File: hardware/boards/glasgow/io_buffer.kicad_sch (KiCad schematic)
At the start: 68 parts, among them J2 IDC-Header_2x10_P2.54mm, J8 Conn_01x08, J9 Conn_01x08, U10 SN74LVC1T45DCKR, U11 SN74LVC1T45DCKR, U16 SN74LVC1T45DCKR, U17 SN74LVC1T45DCKR, U18 SN74LVC1T45DCKR, U19 PCA6408APW, U20 DAC081C081CIMK, U21 INA233, U31 TPS73101DBV, U4 SN74LVC1T45DCKR, U6 SN74LVC1T45DCKR, U9 SN74LVC1T45DCKR

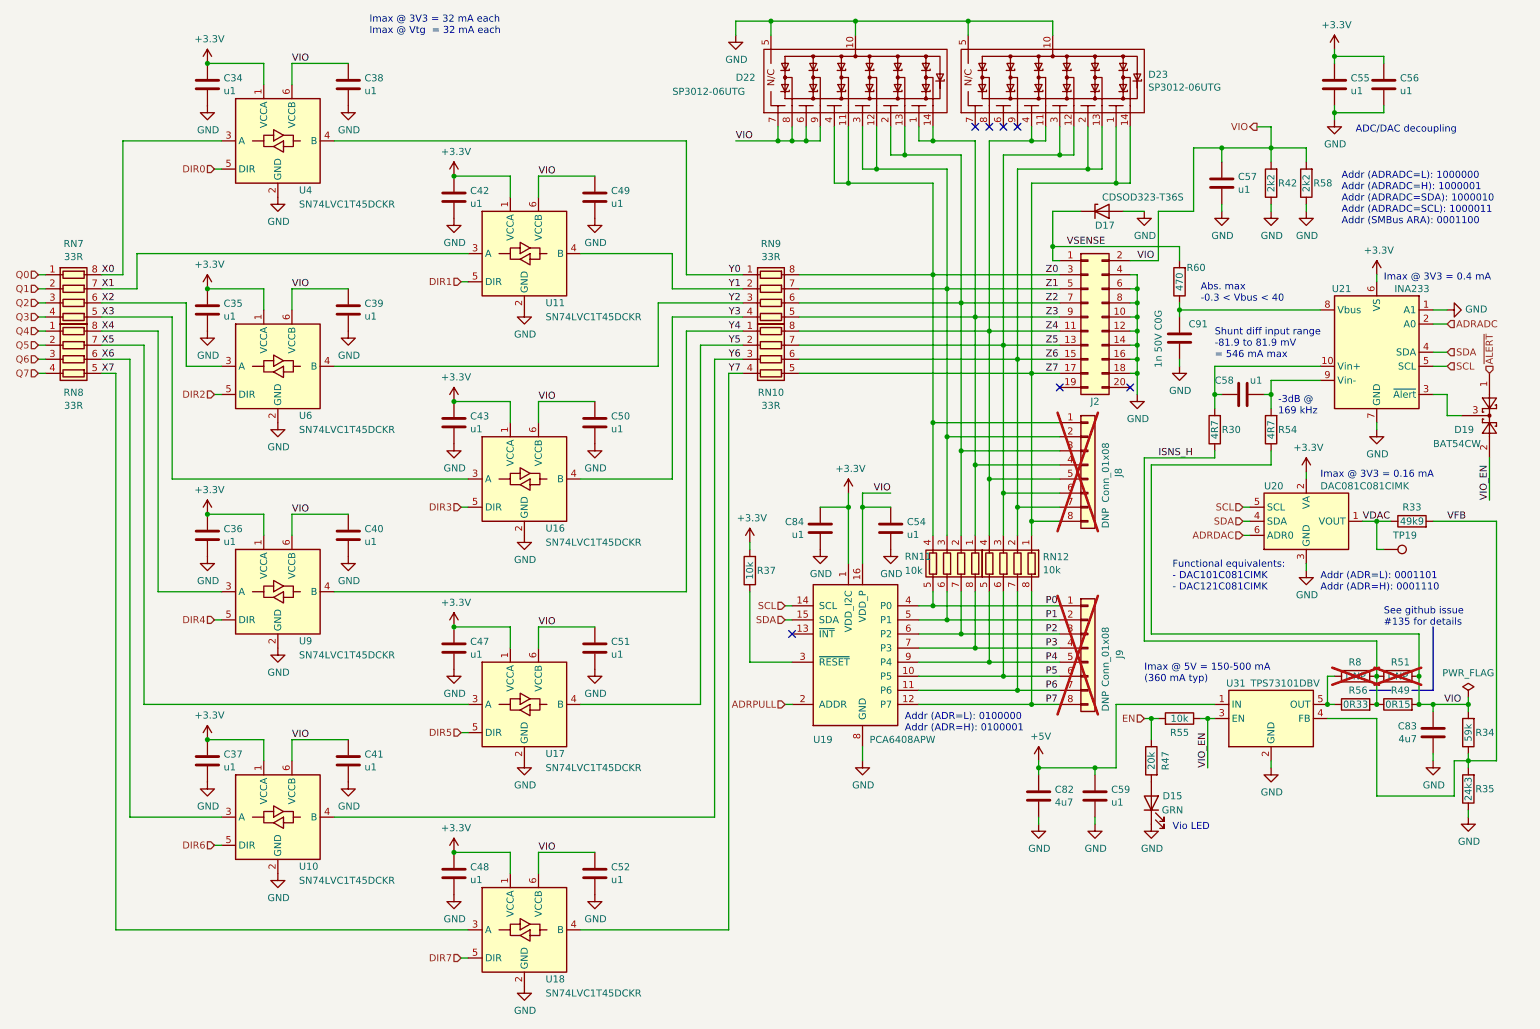
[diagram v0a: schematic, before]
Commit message: JLCPCB part swaps
Switch parts to be either of:
- cheaper
- in stock
- order-able
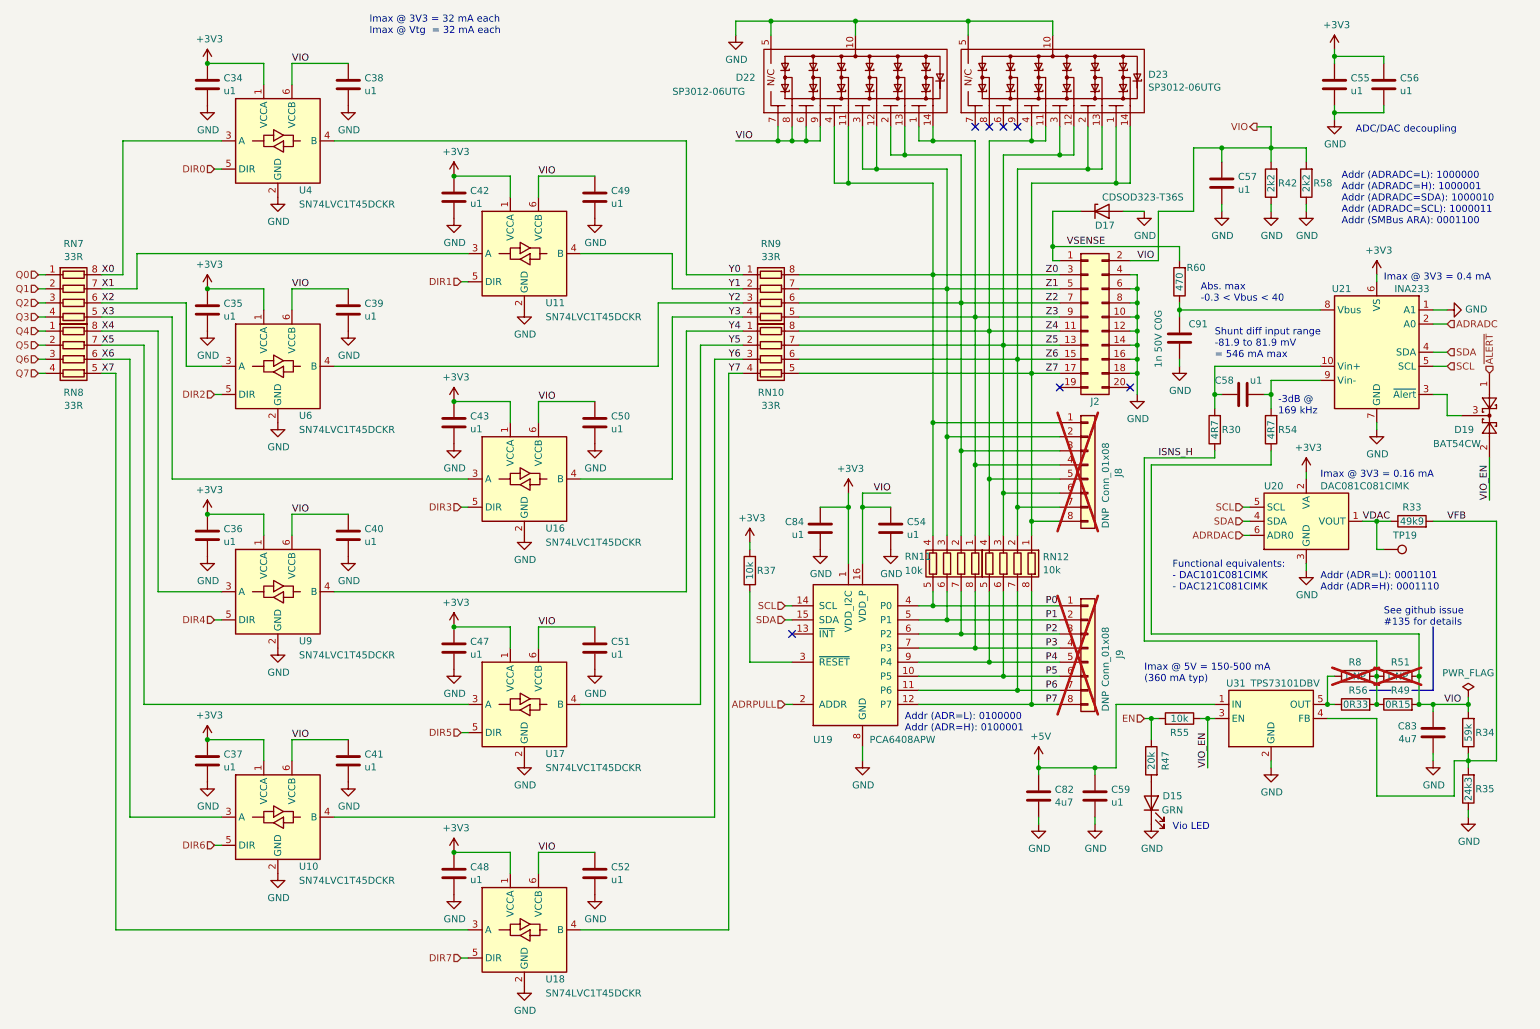
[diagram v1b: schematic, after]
